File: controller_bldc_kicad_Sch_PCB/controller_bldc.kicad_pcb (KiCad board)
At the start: 2 copper layers, 178.1 x 101.9 mm, 57 parts, among them J1 Battery Supply, J2 Emergency Button OUT, J3 Emergency Button IN, J4 Brake, J5 Throttle, J6 LM35, J7 Hall Sensors, J8 Nextion Nx3224T028, J9 BLDC Motor, K1 ADW11, Q1 IRF1010N, Q2 IRF1010N, Q3 IRF1010N, Q4 IRF1010N, Q5 IRF1010N, Q6 IRF1010N, SW1 ON_OFF, SW2 OPC, U1 ESP32-DEVKITC-32D, U2 LM317_TO-220, U3 LM7805_TO220, U4 IR2103, U8 IR2103, U9 IR2103

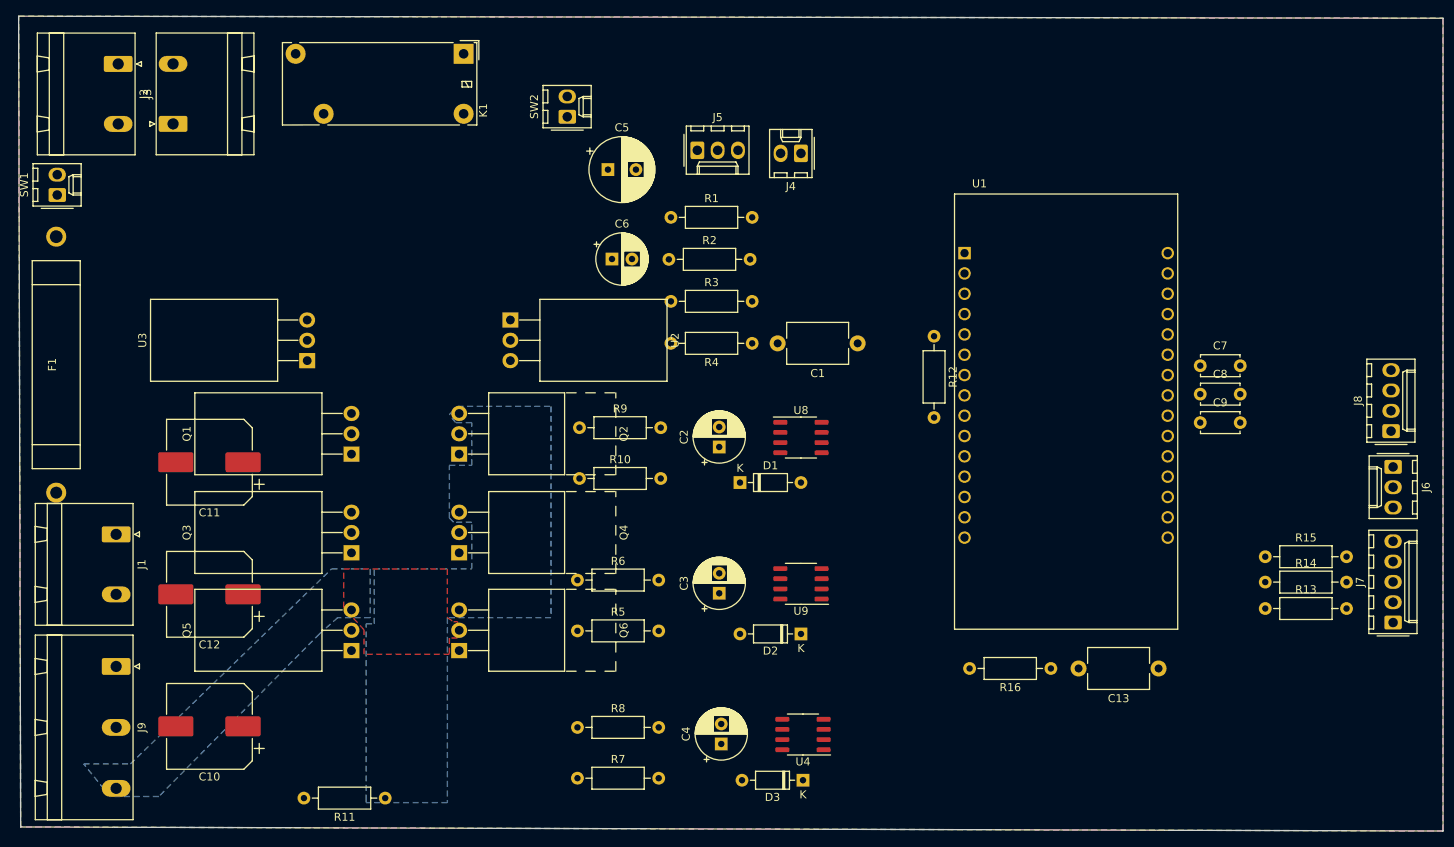
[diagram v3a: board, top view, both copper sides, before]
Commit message: This is with previous tracks, so 2mm are kept but narrowers are deleted. Version before autorouting
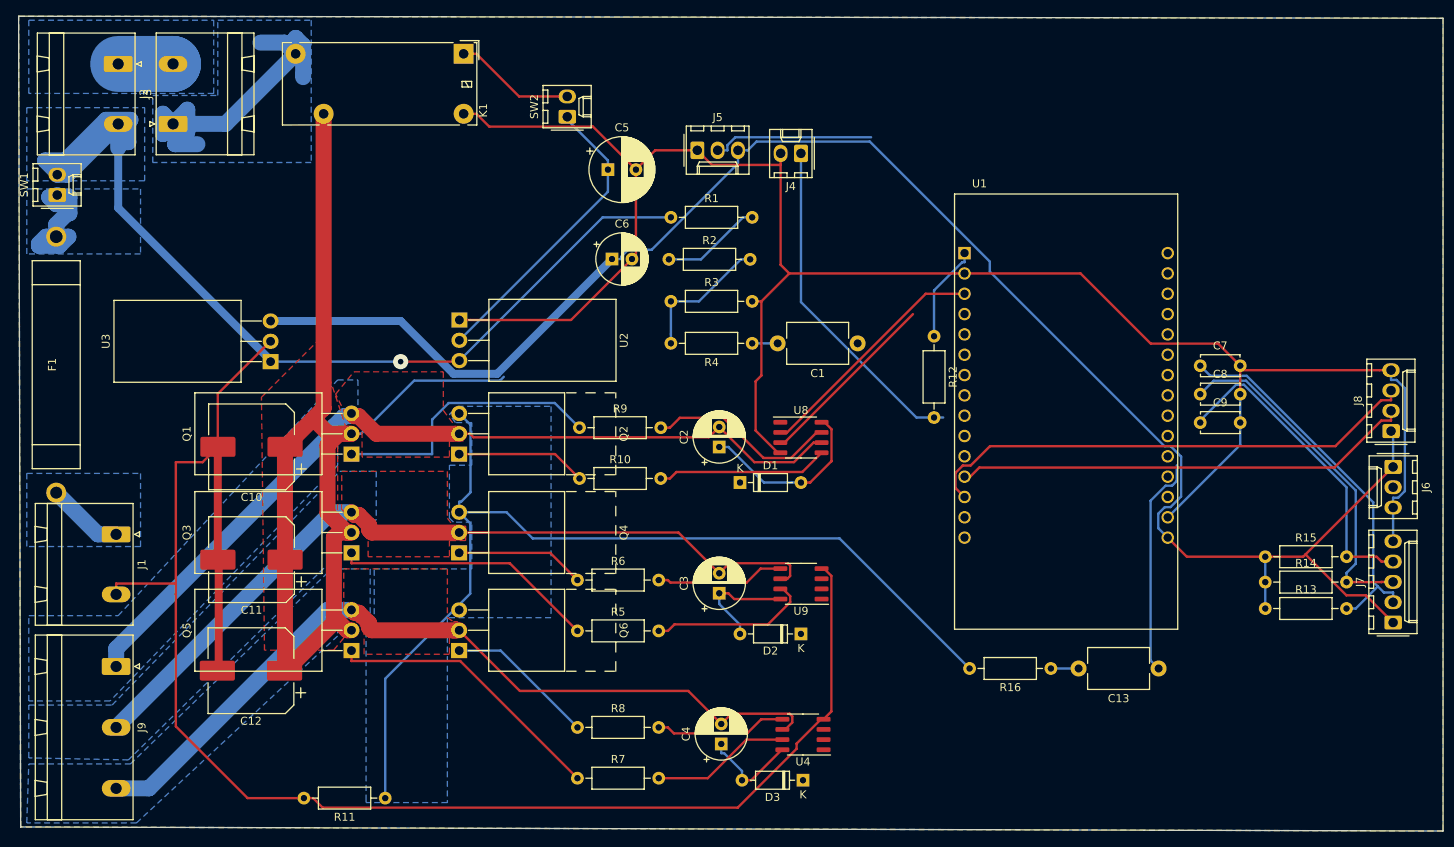
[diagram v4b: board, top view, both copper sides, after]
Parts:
- moved C10 35.3 mm to (130.7, 128.8)
- moved C11 13.3 mm to (130.7, 142.9)
- moved C12 10.9 mm to (130.6, 156.7)
- moved U2 6.38 mm to (156.7, 112.9)
- moved U3 4.57 mm to (133.1, 118.1)
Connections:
- C10 pad 1: +36V -> 36V-Power
- C11 pad 1: +36V -> 36V-Power
- C12 pad 1: +36V -> 36V-Power
- U1 pad 10: Brake -> LM35
- U1 pad 11: (no net) -> Brake
- U1 pad 22: HALL-A -> (no net)
- U1 pad 23: HALL-B -> HALL-A
- U1 pad 24: HALL-C -> HALL-B
- U1 pad 25: Throttle -> HALL-C
- U1 pad 26: Current_Sensor_IN -> Throttle
- U1 pad 27: Voltage_Sensor -> Current_Sensor_IN
- U1 pad 28: (no net) -> Voltage_Sensor
- U1 pad 4: LIN1 -> (no net)
- U1 pad 5: HIN2 -> LIN1
- U1 pad 6: LIN2 -> HIN2
- U1 pad 7: HIN3 -> LIN2
- U1 pad 8: LIN3 -> HIN3
- U1 pad 9: LM35 -> LIN3
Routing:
- net GND: track 0.00 -> 450.7 mm
- net +5V: track 0.00 -> 218.3 mm
- net 36V-Power: track 0.00 -> 139.7 mm
- net +36V: track 0.00 -> 138.2 mm, vias 0 -> 1
- net Current_Sensor: track 0.00 -> 126.9 mm
- net PH1: track 0.00 -> 107.5 mm
- net PH3: track 0.00 -> 103.0 mm
- net PH2: track 0.00 -> 102.2 mm
- net RX-LCD: track 0.00 -> 62.9 mm
- net TX-LCD: track 0.00 -> 57.4 mm
- net HALL-A: track 0.00 -> 47.9 mm
- net Net-(J3-Pad1): track 0.00 -> 47.6 mm
- net HALL-B: track 0.00 -> 43.8 mm
- net Brake: track 0.00 -> 42.4 mm
- net HALL-C: track 0.00 -> 40.4 mm
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- added copper zone on B.Cu, net +36V
- added copper zone on F.Cu, net 36V-Power
- added copper zone on B.Cu, net Net-(F1-Pad1)
- added copper zone on B.Cu, net Net-(F1-Pad2)
- added copper zone on B.Cu, net Net-(J2-Pad1)
- added copper zone on B.Cu, net Net-(J3-Pad1)
- added copper zone on B.Cu, net PH1
- added copper zone on F.Cu, net PH1
- added copper zone on B.Cu, net PH2
- added copper zone on F.Cu, net PH2

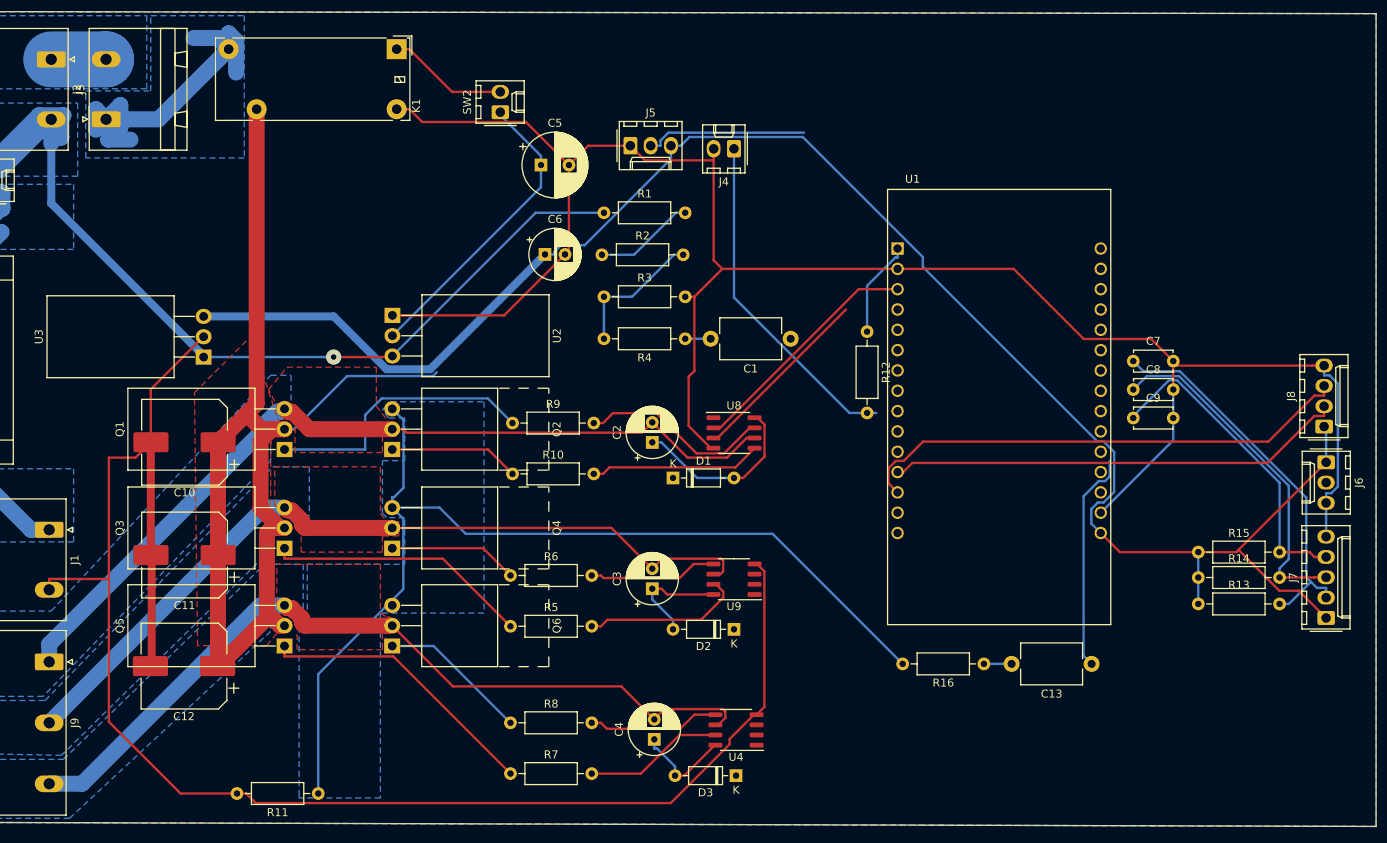
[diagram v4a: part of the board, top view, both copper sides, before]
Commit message: Deleted unblocked routes to be processed by FreeRouting
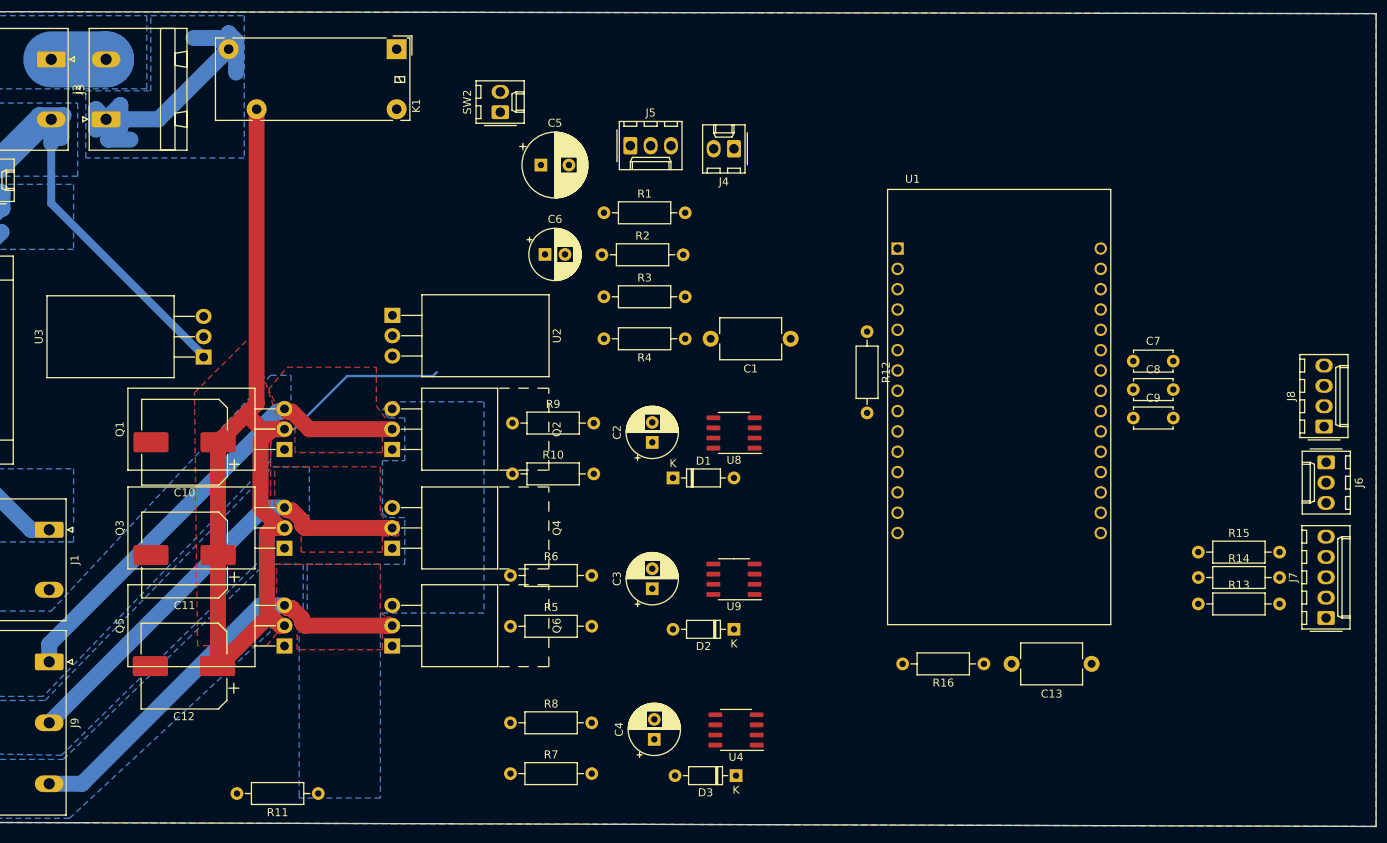
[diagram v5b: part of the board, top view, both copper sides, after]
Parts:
- turned U8 to 180 degrees
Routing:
- net GND: track 450.7 -> 0.00 mm
- net +5V: track 218.3 -> 0.00 mm
- net Current_Sensor: track 126.9 -> 0.00 mm
- net RX-LCD: track 62.9 -> 0.00 mm
- net +36V: track 138.2 -> 80.7 mm, vias 1 -> 0
- net TX-LCD: track 57.4 -> 0.00 mm
- net PH3: track 103.0 -> 53.5 mm
- net PH1: track 107.5 -> 58.6 mm
- net HALL-A: track 47.9 -> 0.00 mm
- net PH2: track 102.2 -> 55.4 mm
- net HALL-B: track 43.8 -> 0.00 mm
- net Brake: track 42.4 -> 0.00 mm
- net HALL-C: track 40.4 -> 0.00 mm
- net +12V: track 37.7 -> 0.00 mm
- net Net-(Q5-Pad1): track 35.6 -> 0.00 mm
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
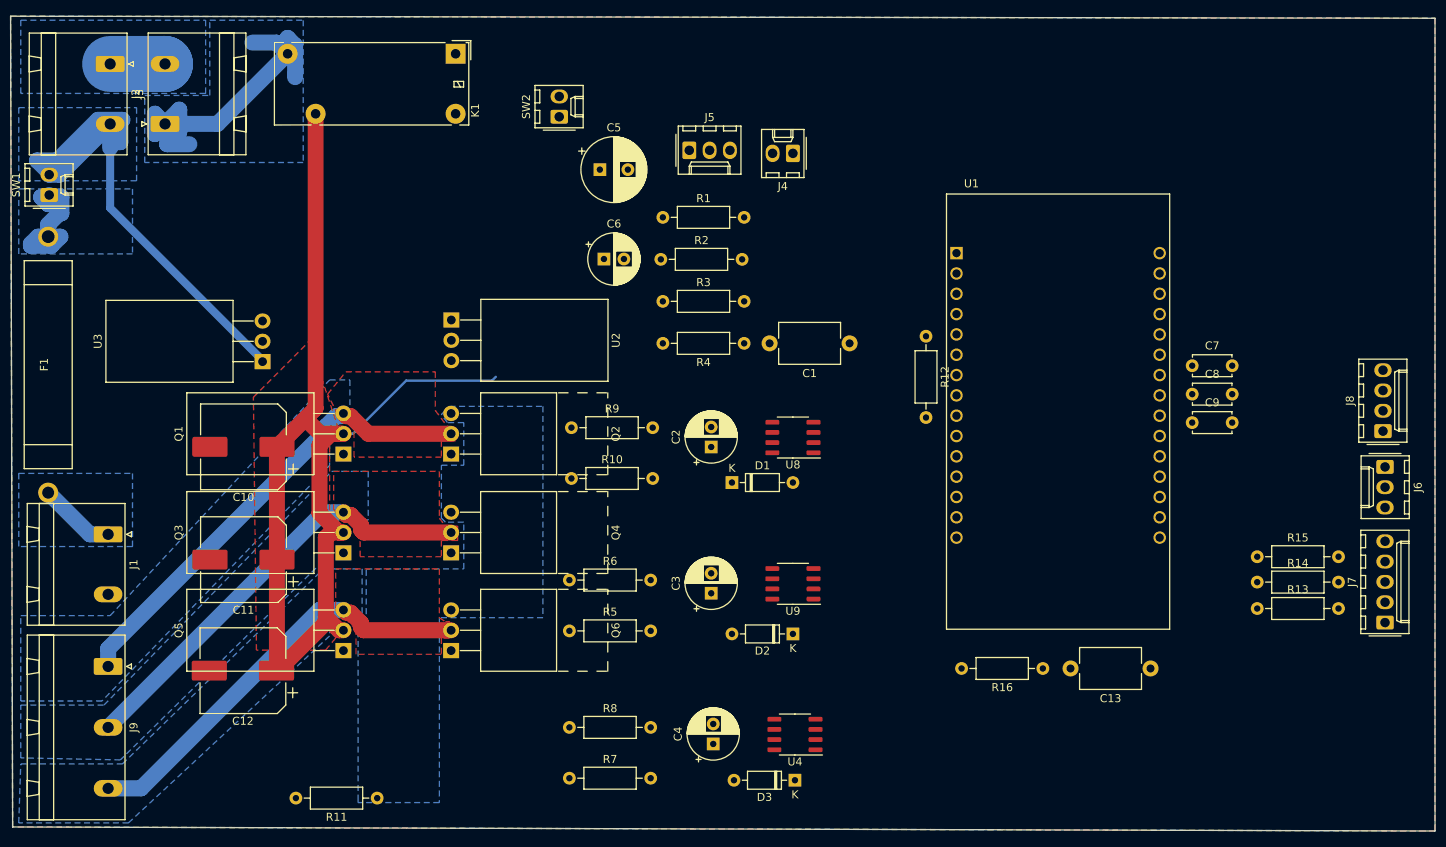
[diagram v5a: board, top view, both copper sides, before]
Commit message: PCB v0.9 after Freerouting, only remaining the verification of the relay. Remember connectors, the fuse and the code for the screen, sensors, current control and also the design and manufacture of the OPC
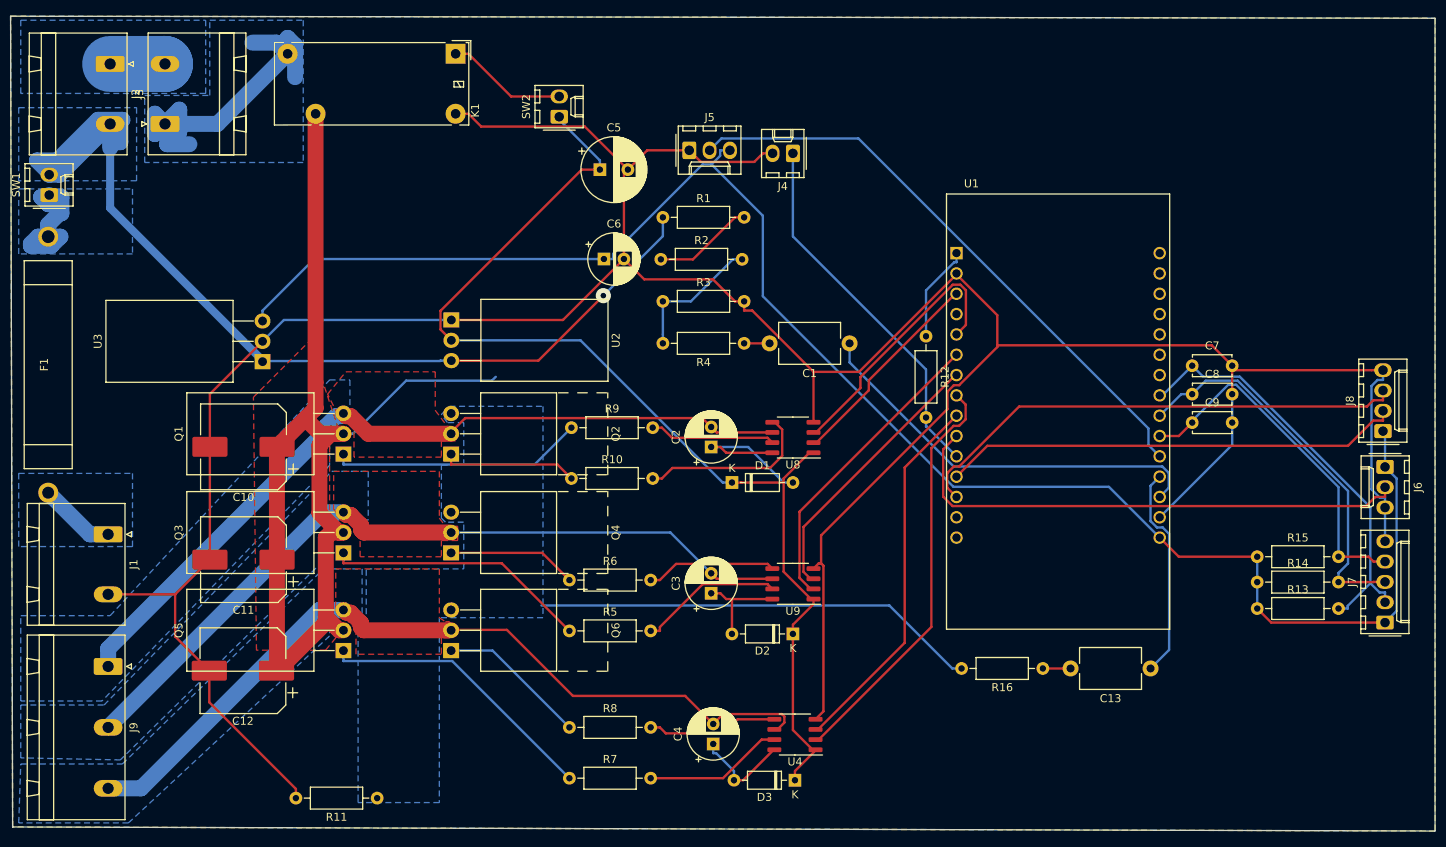
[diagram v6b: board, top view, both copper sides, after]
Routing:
- net GND: track 0.00 -> 405.6 mm
- net +5V: track 0.00 -> 211.6 mm
- net +12V: track 0.00 -> 137.1 mm
- net Throttle: track 0.00 -> 74.6 mm
- net LM35: track 0.00 -> 65.7 mm
- net RX-LCD: track 0.00 -> 62.9 mm
- net +36V: track 80.7 -> 139.6 mm, vias 0 -> 1
- net TX-LCD: track 0.00 -> 57.4 mm
- net Current_Sensor: track 0.00 -> 55.8 mm
- net HALL-A: track 0.00 -> 53.7 mm
- net HIN3: track 0.00 -> 51.9 mm
- net Voltage_Sensor: track 0.00 -> 51.5 mm
- net PH3: track 53.5 -> 103.5 mm
- net HALL-B: track 0.00 -> 48.8 mm
- net LIN3: track 0.00 -> 46.7 mm
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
